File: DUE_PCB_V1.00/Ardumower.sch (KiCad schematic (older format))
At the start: 54 parts, among them J1 9V IN, J10 Sonar_R, J11 Sonar_C, J12 Sonar_L, J13 P_Right, J14 Buzzer, J15 Button, J16 Button, J17 Button, J18 Button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

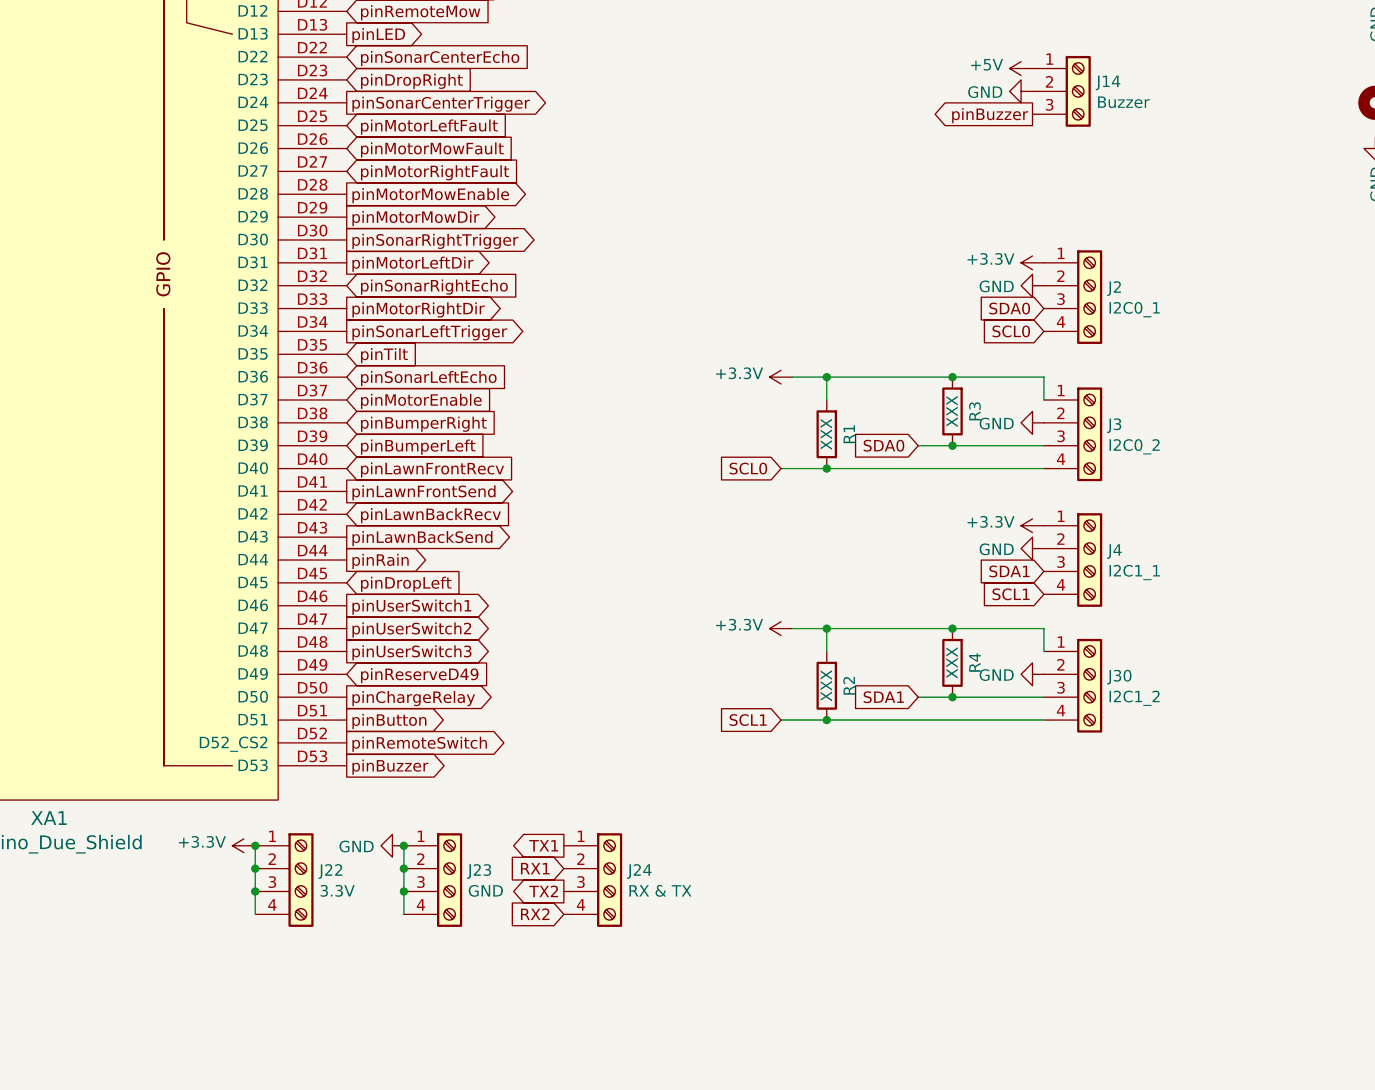
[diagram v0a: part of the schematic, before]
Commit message: Add Ser0-Ser3
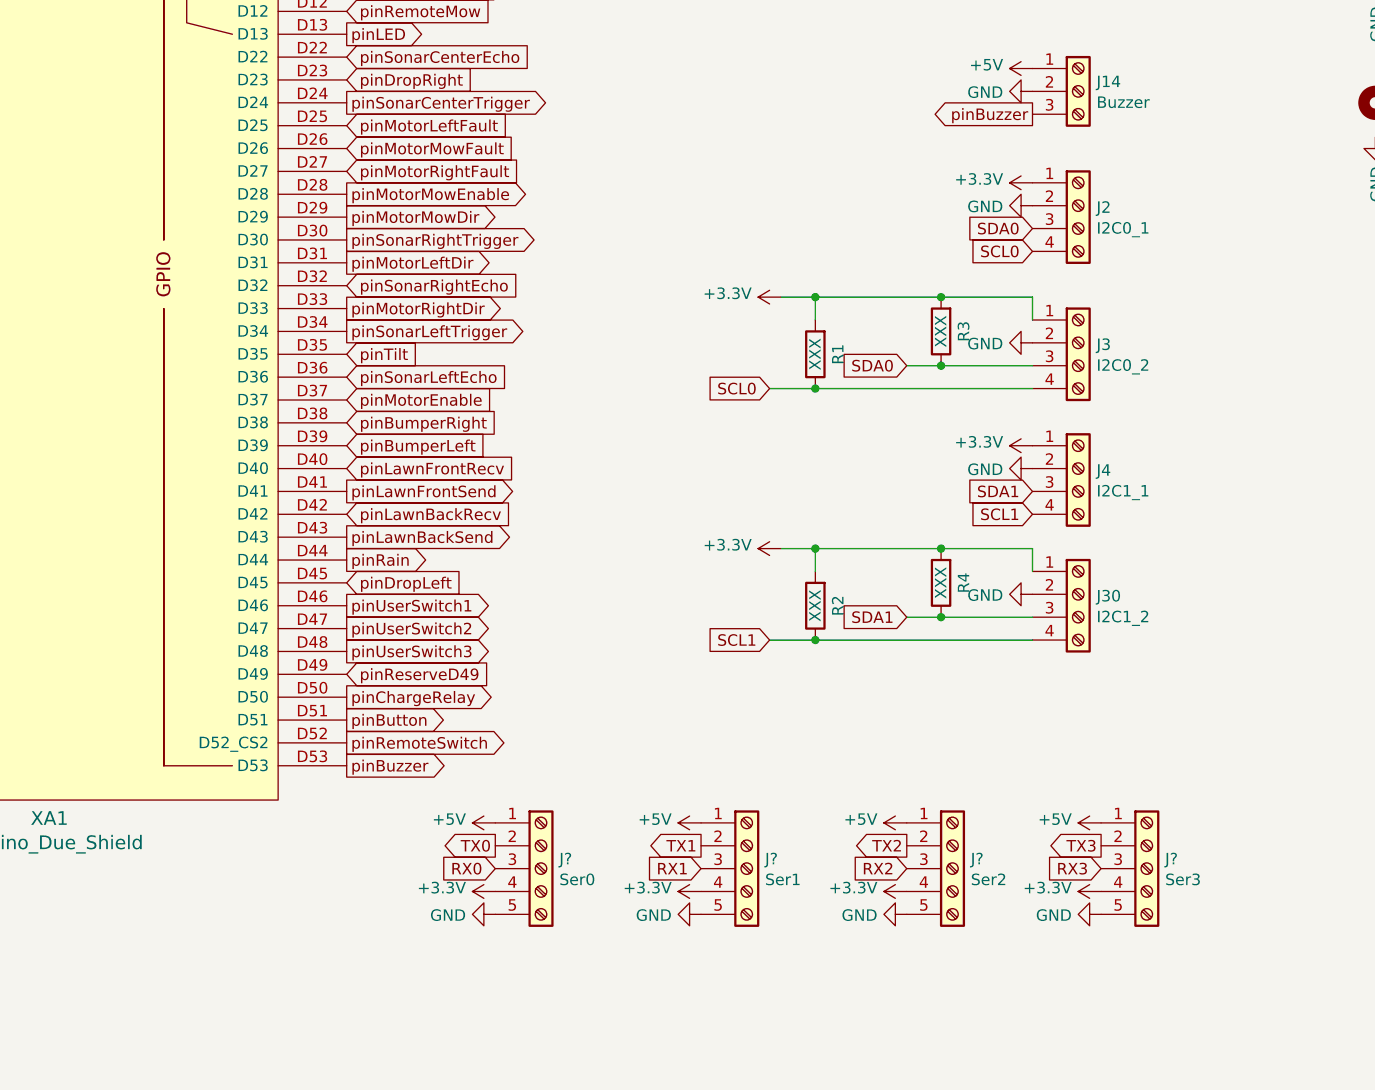
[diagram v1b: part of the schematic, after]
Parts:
- removed J22: 3.3V, Connector_PinHeader_2.54mm:PinHeader_1x04_P2.54mm_Vertical, symbol Connector:Screw_Terminal_01x04
- removed J23: GND, Connector_PinHeader_2.54mm:PinHeader_1x04_P2.54mm_Vertical, symbol Connector:Screw_Terminal_01x04
- removed J24: RX & TX, Connector_PinHeader_2.54mm:PinHeader_1x04_P2.54mm_Vertical, symbol Connector:Screw_Terminal_01x04
- added J?: Ser1, symbol Connector:Screw_Terminal_01x05
- added J?: Ser2, symbol Connector:Screw_Terminal_01x05
- added J?: Ser0, symbol Connector:Screw_Terminal_01x05
- added J?: Ser3, symbol Connector:Screw_Terminal_01x05
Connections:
- net +3V3: now also J?.4 (Pin_4), J?.4 (Pin_4), J?.4 (Pin_4), J?.4 (Pin_4)
- net +5V: now also J?.1 (Pin_1), J?.1 (Pin_1), J?.1 (Pin_1), J?.1 (Pin_1)
- net GND: now also J?.5 (Pin_5), J?.5 (Pin_5), J?.5 (Pin_5), J?.5 (Pin_5)
- net RX0: now also J?.3 (Pin_3)
- net RX1: now also J?.3 (Pin_3)
- net RX2: now also J?.3 (Pin_3)
- net RX3: now also J?.3 (Pin_3)
- net TX0: now also J?.2 (Pin_2)
- net TX1: now also J?.2 (Pin_2)
- net TX2: now also J?.2 (Pin_2)
- net TX3: now also J?.2 (Pin_2)
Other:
- moved on the sheet: J2, J3, J30, J4, R1, R2, R3, R4

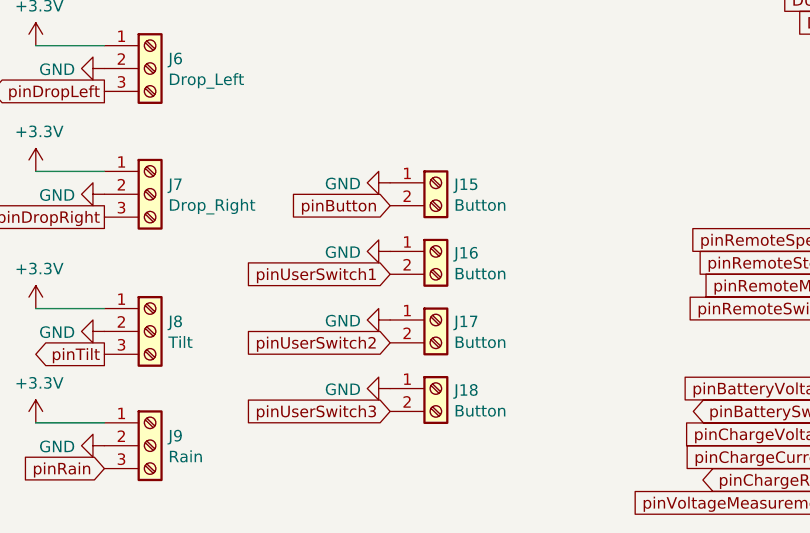
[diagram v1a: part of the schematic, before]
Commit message: Rename Button to US1-US3
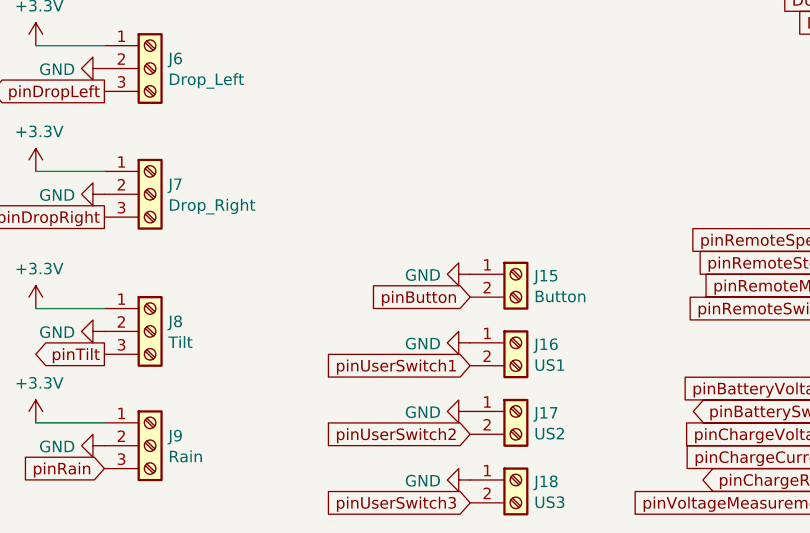
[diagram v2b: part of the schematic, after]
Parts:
- J16: value Button -> US1
- J17: value Button -> US2
- J18: value Button -> US3
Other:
- moved on the sheet: J15, J16, J17, J18
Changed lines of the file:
@@
 L Connector:Screw_Terminal_01x02 J15
 U 1 1 607D1A82
-P 2900 6200
-F 0 "J15" H 2980 6192 50  0000 L CNN
-F 1 "Button" H 2980 6101 50  0000 L CNN
-F 2 "Zimprich:Pin_Header_KK110_1x02_3D" H 2900 6200 50  0001 C CNN
-F 3 "~" H 2900 6200 50  0001 C CNN
-	1    2900 6200
-	1    0    0    -1
-$EndComp
-Text GLabel 2700 6300 0    50   Input ~ 0
+P 3250 6600
+F 0 "J15" H 3330 6592 50  0000 L CNN
+F 1 "Button" H 3330 6501 50  0000 L CNN
+F 2 "Zimprich:Pin_Header_KK110_1x02_3D" H 3250 6600 50  0001 C CNN
+F 3 "~" H 3250 6600 50  0001 C CNN
+	1    3250 6600
+	1    0    0    -1
+$EndComp
+Text GLabel 3050 6700 0    50   Input ~ 0
 pinButton
 $Comp
@@
 L power:GND #PWR030
 U 1 1 60978B23
-P 2700 6200
-F 0 "#PWR030" H 2700 5950 50  0001 C CNN
-F 1 "GND" V 2705 6072 50  0000 R CNN
-F 2 "" H 2700 6200 50  0001 C CNN
-F 3 "" H 2700 6200 50  0001 C CNN
-	1    2700 6200
+P 3050 6600
+F 0 "#PWR030" H 3050 6350 50  0001 C CNN
+F 1 "GND" V 3055 6472 50  0000 R CNN
+F 2 "" H 3050 6600 50  0001 C CNN
+F 3 "" H 3050 6600 50  0001 C CNN
+	1    3050 6600
 	0    1    1    0
 $EndComp
@@
 L Connector:Screw_Terminal_01x02 J16
 U 1 1 608FC19B
-P 2900 6500
-F 0 "J16" H 2980 6492 50  0000 L CNN
-F 1 "Button" H 2980 6401 50  0000 L CNN
-F 2 "Zimprich:Pin_Header_KK110_1x02_3D" H 2900 6500 50  0001 C CNN
-F 3 "~" H 2900 6500 50  0001 C CNN
-	1    2900 6500
-	1    0    0    -1
-$EndComp
-Text GLabel 2700 6600 0    50   Input ~ 0
+P 3250 6900
+F 0 "J16" H 3330 6892 50  0000 L CNN
+F 1 "US1" H 3330 6801 50  0000 L CNN
+F 2 "Zimprich:Pin_Header_KK110_1x02_3D" H 3250 6900 50  0001 C CNN
+F 3 "~" H 3250 6900 50  0001 C CNN
+	1    3250 6900
+	1    0    0    -1
+$EndComp
+Text GLabel 3050 7000 0    50   Input ~ 0
 pinUserSwitch1
 $Comp
 L power:GND #PWR031
 U 1 1 608FCDEE
-P 2700 6500
-F 0 "#PWR031" H 2700 6250 50  0001 C CNN
-F 1 "GND" V 2705 6372 50  0000 R CNN
-F 2 "" H 2700 6500 50  0001 C CNN
-F 3 "" H 2700 6500 50  0001 C CNN
-	1    2700 6500
+P 3050 6900
+F 0 "#PWR031" H 3050 6650 50  0001 C CNN
+F 1 "GND" V 3055 6772 50  0000 R CNN
+F 2 "" H 3050 6900 50  0001 C CNN
+F 3 "" H 3050 6900 50  0001 C CNN
+	1    3050 6900
 	0    1    1    0
 $EndComp
@@
 L Connector:Screw_Terminal_01x02 J17
 U 1 1 609039FE
-P 2900 6800
-F 0 "J17" H 2980 6792 50  0000 L CNN
-F 1 "Button" H 2980 6701 50  0000 L CNN
-F 2 "Zimprich:Pin_Header_KK110_1x02_3D" H 2900 6800 50  0001 C CNN
-F 3 "~" H 2900 6800 50  0001 C CNN
-	1    2900 6800
-	1    0    0    -1
-$EndComp
-Text GLabel 2700 6900 0    50   Input ~ 0
+P 3250 7200
+F 0 "J17" H 3330 7192 50  0000 L CNN
+F 1 "US2" H 3330 7101 50  0000 L CNN
+F 2 "Zimprich:Pin_Header_KK110_1x02_3D" H 3250 7200 50  0001 C CNN
+F 3 "~" H 3250 7200 50  0001 C CNN
+	1    3250 7200
+	1    0    0    -1
+$EndComp
+Text GLabel 3050 7300 0    50   Input ~ 0
 pinUserSwitch2
 $Comp
 L power:GND #PWR032
 U 1 1 60904679
-P 2700 6800
-F 0 "#PWR032" H 2700 6550 50  0001 C CNN
-F 1 "GND" V 2705 6672 50  0000 R CNN
-F 2 "" H 2700 6800 50  0001 C CNN
-F 3 "" H 2700 6800 50  0001 C CNN
-	1    2700 6800
+P 3050 7200
+F 0 "#PWR032" H 3050 6950 50  0001 C CNN
+F 1 "GND" V 3055 7072 50  0000 R CNN
+F 2 "" H 3050 7200 50  0001 C CNN
+F 3 "" H 3050 7200 50  0001 C CNN
+	1    3050 7200
 	0    1    1    0
 $EndComp
@@
 L Connector:Screw_Terminal_01x02 J18
 U 1 1 6090A18A
-P 2900 7100
-F 0 "J18" H 2980 7092 50  0000 L CNN
-F 1 "Button" H 2980 7001 50  0000 L CNN
-F 2 "Zimprich:Pin_Header_KK110_1x02_3D" H 2900 7100 50  0001 C CNN
-F 3 "~" H 2900 7100 50  0001 C CNN
-	1    2900 7100
-	1    0    0    -1
-$EndComp
-Text GLabel 2700 7200 0    50   Input ~ 0
+P 3250 7500
+F 0 "J18" H 3330 7492 50  0000 L CNN
+F 1 "US3" H 3330 7401 50  0000 L CNN
+F 2 "Zimprich:Pin_Header_KK110_1x02_3D" H 3250 7500 50  0001 C CNN
+F 3 "~" H 3250 7500 50  0001 C CNN
+	1    3250 7500
+	1    0    0    -1
+$EndComp
+Text GLabel 3050 7600 0    50   Input ~ 0
 pinUserSwitch3
 $Comp
 L power:GND #PWR033
 U 1 1 6090AE2D
-P 2700 7100
-F 0 "#PWR033" H 2700 6850 50  0001 C CNN
-F 1 "GND" V 2705 6972 50  0000 R CNN
-F 2 "" H 2700 7100 50  0001 C CNN
-F 3 "" H 2700 7100 50  0001 C CNN
-	1    2700 7100
-	0    1    1    0
-$EndComp
+P 3050 7500
+F 0 "#PWR033" H 3050 7250 50  0001 C CNN
+F 1 "GND" V 3055 7372 50  0000 R CNN
+F 2 "" H 3050 7500 50  0001 C CNN
+F 3 "" H 3050 7500 50  0001 C CNN
+	1    3050 7500
+	0    1    1    0
+$EndComp

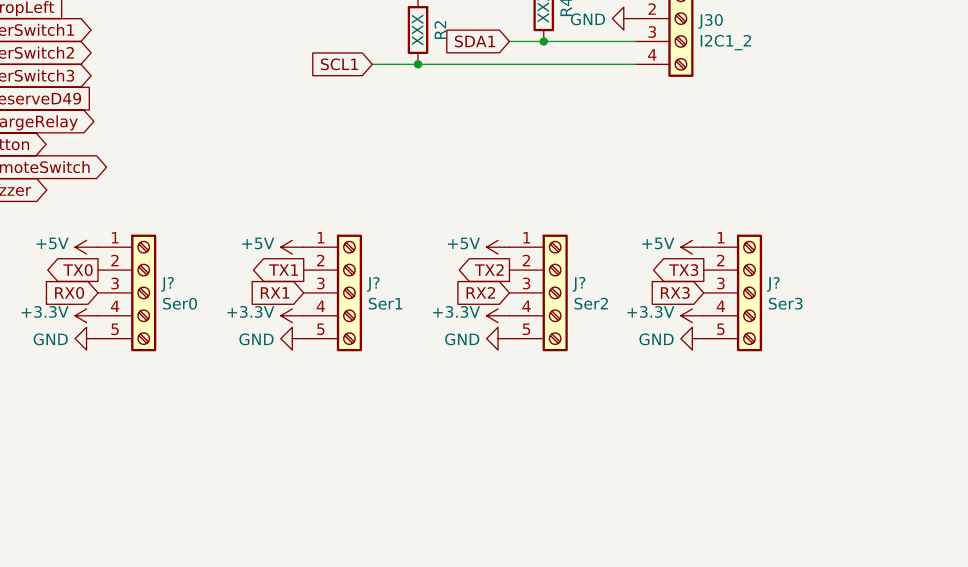
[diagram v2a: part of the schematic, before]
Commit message: Add Footprint for Ser0-Ser3
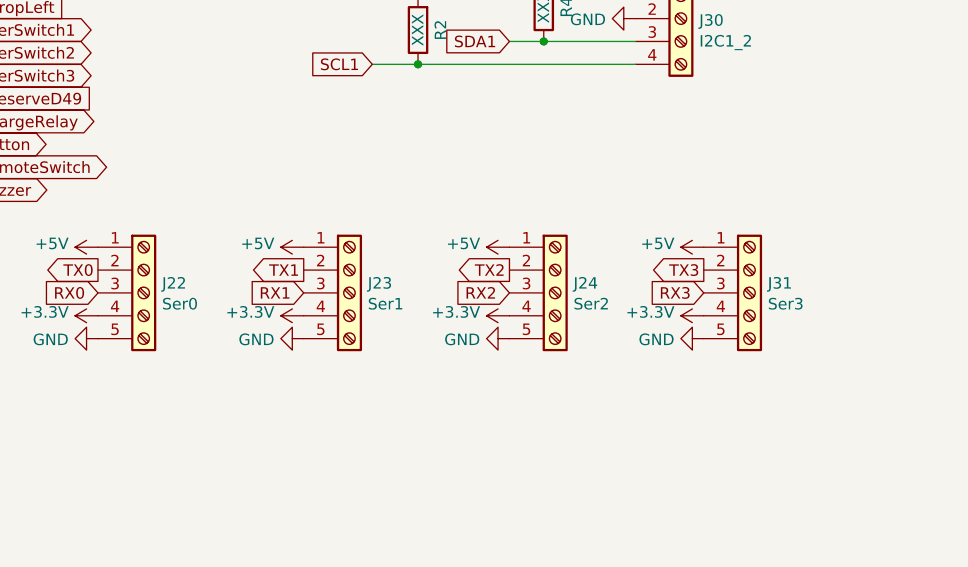
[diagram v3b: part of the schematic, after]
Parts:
- J15, J16, J17, J18: footprint Zimprich:Pin_Header_KK110_1x02_3D -> Connector_PinHeader_2.54mm:PinHeader_1x02_P2.54mm_Vertical
- J22, J23, J24, J31: renamed from J?; footprint (none) -> Connector_PinHeader_2.54mm:PinHeader_1x05_P2.54mm_Vertical
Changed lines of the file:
@@
 F 0 "J15" H 3330 6592 50  0000 L CNN
 F 1 "Button" H 3330 6501 50  0000 L CNN
-F 2 "Zimprich:Pin_Header_KK110_1x02_3D" H 3250 6600 50  0001 C CNN
+F 2 "Connector_PinHeader_2.54mm:PinHeader_1x02_P2.54mm_Vertical" H 3250 6600 50  0001 C CNN
 F 3 "~" H 3250 6600 50  0001 C CNN
 	1    3250 6600
@@
 F 0 "J16" H 3330 6892 50  0000 L CNN
 F 1 "US1" H 3330 6801 50  0000 L CNN
-F 2 "Zimprich:Pin_Header_KK110_1x02_3D" H 3250 6900 50  0001 C CNN
+F 2 "Connector_PinHeader_2.54mm:PinHeader_1x02_P2.54mm_Vertical" H 3250 6900 50  0001 C CNN
 F 3 "~" H 3250 6900 50  0001 C CNN
 	1    3250 6900
@@
 F 0 "J17" H 3330 7192 50  0000 L CNN
 F 1 "US2" H 3330 7101 50  0000 L CNN
-F 2 "Zimprich:Pin_Header_KK110_1x02_3D" H 3250 7200 50  0001 C CNN
+F 2 "Connector_PinHeader_2.54mm:PinHeader_1x02_P2.54mm_Vertical" H 3250 7200 50  0001 C CNN
 F 3 "~" H 3250 7200 50  0001 C CNN
 	1    3250 7200
@@
 F 0 "J18" H 3330 7492 50  0000 L CNN
 F 1 "US3" H 3330 7401 50  0000 L CNN
-F 2 "Zimprich:Pin_Header_KK110_1x02_3D" H 3250 7500 50  0001 C CNN
+F 2 "Connector_PinHeader_2.54mm:PinHeader_1x02_P2.54mm_Vertical" H 3250 7500 50  0001 C CNN
 F 3 "~" H 3250 7500 50  0001 C CNN
 	1    3250 7500
@@
 	9500 4850 9350 4850
 $Comp
-L Connector:Screw_Terminal_01x05 J?
+L Connector:Screw_Terminal_01x05 J23
 U 1 1 60D8BA62
 P 9200 6250
-F 0 "J?" H 9280 6292 50  0000 L CNN
+F 0 "J23" H 9280 6292 50  0000 L CNN
 F 1 "Ser1" H 9280 6201 50  0000 L CNN
-F 2 "" H 9200 6250 50  0001 C CNN
+F 2 "Connector_PinHeader_2.54mm:PinHeader_1x05_P2.54mm_Vertical" H 9200 6250 50  0001 C CNN
 F 3 "~" H 9200 6250 50  0001 C CNN
 	1    9200 6250
@@
 $EndComp
 $Comp
-L power:+3.3V #PWR?
+L power:+3.3V #PWR073
 U 1 1 60D8E37F
 P 9000 6350
-F 0 "#PWR?" H 9000 6200 50  0001 C CNN
+F 0 "#PWR073" H 9000 6200 50  0001 C CNN
 F 1 "+3.3V" V 9015 6478 50  0000 L CNN
 F 2 "" H 9000 6350 50  0001 C CNN
@@
 $EndComp
 $Comp
-L power:GND #PWR?
+L power:GND #PWR074
 U 1 1 60D8F6A0
 P 9000 6450
-F 0 "#PWR?" H 9000 6200 50  0001 C CNN
+F 0 "#PWR074" H 9000 6200 50  0001 C CNN
 F 1 "GND" V 9005 6322 50  0000 R CNN
 F 2 "" H 9000 6450 50  0001 C CNN
@@
 $EndComp
 $Comp
-L power:+5V #PWR?
+L power:+5V #PWR072
 U 1 1 60D9058A
 P 9000 6050
-F 0 "#PWR?" H 9000 5900 50  0001 C CNN
+F 0 "#PWR072" H 9000 5900 50  0001 C CNN
 F 1 "+5V" V 9015 6178 50  0000 L CNN
 F 2 "" H 9000 6050 50  0001 C CNN
@@
 TX2
 $Comp
-L Connector:Screw_Terminal_01x05 J?
+L Connector:Screw_Terminal_01x05 J24
 U 1 1 60D92B9E
 P 10100 6250
-F 0 "J?" H 10180 6292 50  0000 L CNN
+F 0 "J24" H 10180 6292 50  0000 L CNN
 F 1 "Ser2" H 10180 6201 50  0000 L CNN
-F 2 "" H 10100 6250 50  0001 C CNN
+F 2 "Connector_PinHeader_2.54mm:PinHeader_1x05_P2.54mm_Vertical" H 10100 6250 50  0001 C CNN
 F 3 "~" H 10100 6250 50  0001 C CNN
 	1    10100 6250
@@
 $EndComp
 $Comp
-L power:+3.3V #PWR?
+L power:+3.3V #PWR076
 U 1 1 60D92BA8
 P 9900 6350
-F 0 "#PWR?" H 9900 6200 50  0001 C CNN
+F 0 "#PWR076" H 9900 6200 50  0001 C CNN
 F 1 "+3.3V" V 9915 6478 50  0000 L CNN
 F 2 "" H 9900 6350 50  0001 C CNN
@@
 $EndComp
 $Comp
-L power:GND #PWR?
+L power:GND #PWR077
 U 1 1 60D92BB2
 P 9900 6450
-F 0 "#PWR?" H 9900 6200 50  0001 C CNN
+F 0 "#PWR077" H 9900 6200 50  0001 C CNN
 F 1 "GND" V 9905 6322 50  0000 R CNN
 F 2 "" H 9900 6450 50  0001 C CNN
@@
 $EndComp
 $Comp
-L power:+5V #PWR?
+L power:+5V #PWR075
 U 1 1 60D92BBC
 P 9900 6050
-F 0 "#PWR?" H 9900 5900 50  0001 C CNN
+F 0 "#PWR075" H 9900 5900 50  0001 C CNN
 F 1 "+5V" V 9915 6178 50  0000 L CNN
 F 2 "" H 9900 6050 50  0001 C CNN
@@
 TX0
 $Comp
-L Connector:Screw_Terminal_01x05 J?
+L Connector:Screw_Terminal_01x05 J22
 U 1 1 60D9F760
 P 8300 6250
-F 0 "J?" H 8380 6292 50  0000 L CNN
+F 0 "J22" H 8380 6292 50  0000 L CNN
 F 1 "Ser0" H 8380 6201 50  0000 L CNN
-F 2 "" H 8300 6250 50  0001 C CNN
+F 2 "Connector_PinHeader_2.54mm:PinHeader_1x05_P2.54mm_Vertical" H 8300 6250 50  0001 C CNN
 F 3 "~" H 8300 6250 50  0001 C CNN
 	1    8300 6250
@@
 $EndComp
 $Comp
-L power:+3.3V #PWR?
+L power:+3.3V #PWR045
 U 1 1 60D9F76A
 P 8100 6350
-F 0 "#PWR?" H 8100 6200 50  0001 C CNN
+F 0 "#PWR045" H 8100 6200 50  0001 C CNN
 F 1 "+3.3V" V 8115 6478 50  0000 L CNN
 F 2 "" H 8100 6350 50  0001 C CNN
@@
 $EndComp
 $Comp
-L power:GND #PWR?
+L power:GND #PWR071
 U 1 1 60D9F774
 P 8100 6450
-F 0 "#PWR?" H 8100 6200 50  0001 C CNN
+F 0 "#PWR071" H 8100 6200 50  0001 C CNN
 F 1 "GND" V 8105 6322 50  0000 R CNN
 F 2 "" H 8100 6450 50  0001 C CNN
@@
 $EndComp
 $Comp
-L power:+5V #PWR?
+L power:+5V #PWR044
 U 1 1 60D9F77E
 P 8100 6050
-F 0 "#PWR?" H 8100 5900 50  0001 C CNN
+F 0 "#PWR044" H 8100 5900 50  0001 C CNN
 F 1 "+5V" V 8115 6178 50  0000 L CNN
 F 2 "" H 8100 6050 50  0001 C CNN
@@
 TX3
 $Comp
-L Connector:Screw_Terminal_01x05 J?
+L Connector:Screw_Terminal_01x05 J31
 U 1 1 60DA6EC4
 P 10950 6250
-F 0 "J?" H 11030 6292 50  0000 L CNN
+F 0 "J31" H 11030 6292 50  0000 L CNN
 F 1 "Ser3" H 11030 6201 50  0000 L CNN
-F 2 "" H 10950 6250 50  0001 C CNN
+F 2 "Connector_PinHeader_2.54mm:PinHeader_1x05_P2.54mm_Vertical" H 10950 6250 50  0001 C CNN
 F 3 "~" H 10950 6250 50  0001 C CNN
 	1    10950 6250
@@
 $EndComp
 $Comp
-L power:+3.3V #PWR?
+L power:+3.3V #PWR079
 U 1 1 60DA6ECE
 P 10750 6350
-F 0 "#PWR?" H 10750 6200 50  0001 C CNN
+F 0 "#PWR079" H 10750 6200 50  0001 C CNN
 F 1 "+3.3V" V 10765 6478 50  0000 L CNN
 F 2 "" H 10750 6350 50  0001 C CNN
@@
 $EndComp
 $Comp
-L power:GND #PWR?
+L power:GND #PWR080
 U 1 1 60DA6ED8
 P 10750 6450
-F 0 "#PWR?" H 10750 6200 50  0001 C CNN
+F 0 "#PWR080" H 10750 6200 50  0001 C CNN
 F 1 "GND" V 10755 6322 50  0000 R CNN
 F 2 "" H 10750 6450 50  0001 C CNN
@@
 $EndComp
 $Comp
-L power:+5V #PWR?
+L power:+5V #PWR078
 U 1 1 60DA6EE2
 P 10750 6050
-F 0 "#PWR?" H 10750 5900 50  0001 C CNN
+F 0 "#PWR078" H 10750 5900 50  0001 C CNN
 F 1 "+5V" V 10765 6178 50  0000 L CNN
 F 2 "" H 10750 6050 50  0001 C CNN
